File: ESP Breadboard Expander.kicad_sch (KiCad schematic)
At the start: 18 parts, among them J1 Conn_02x04_Odd_Even, J10 PJ-063BH, J2 Conn_01x08_Socket, J3 Conn_01x08_Socket, J4 Conn_01x19_Socket, J5 Conn_01x19_Socket, J6 Conn_01x14_Pin, J7 Conn_01x14_Pin, J8 Conn_01x02_Socket, J9 Conn_01x02_Socket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

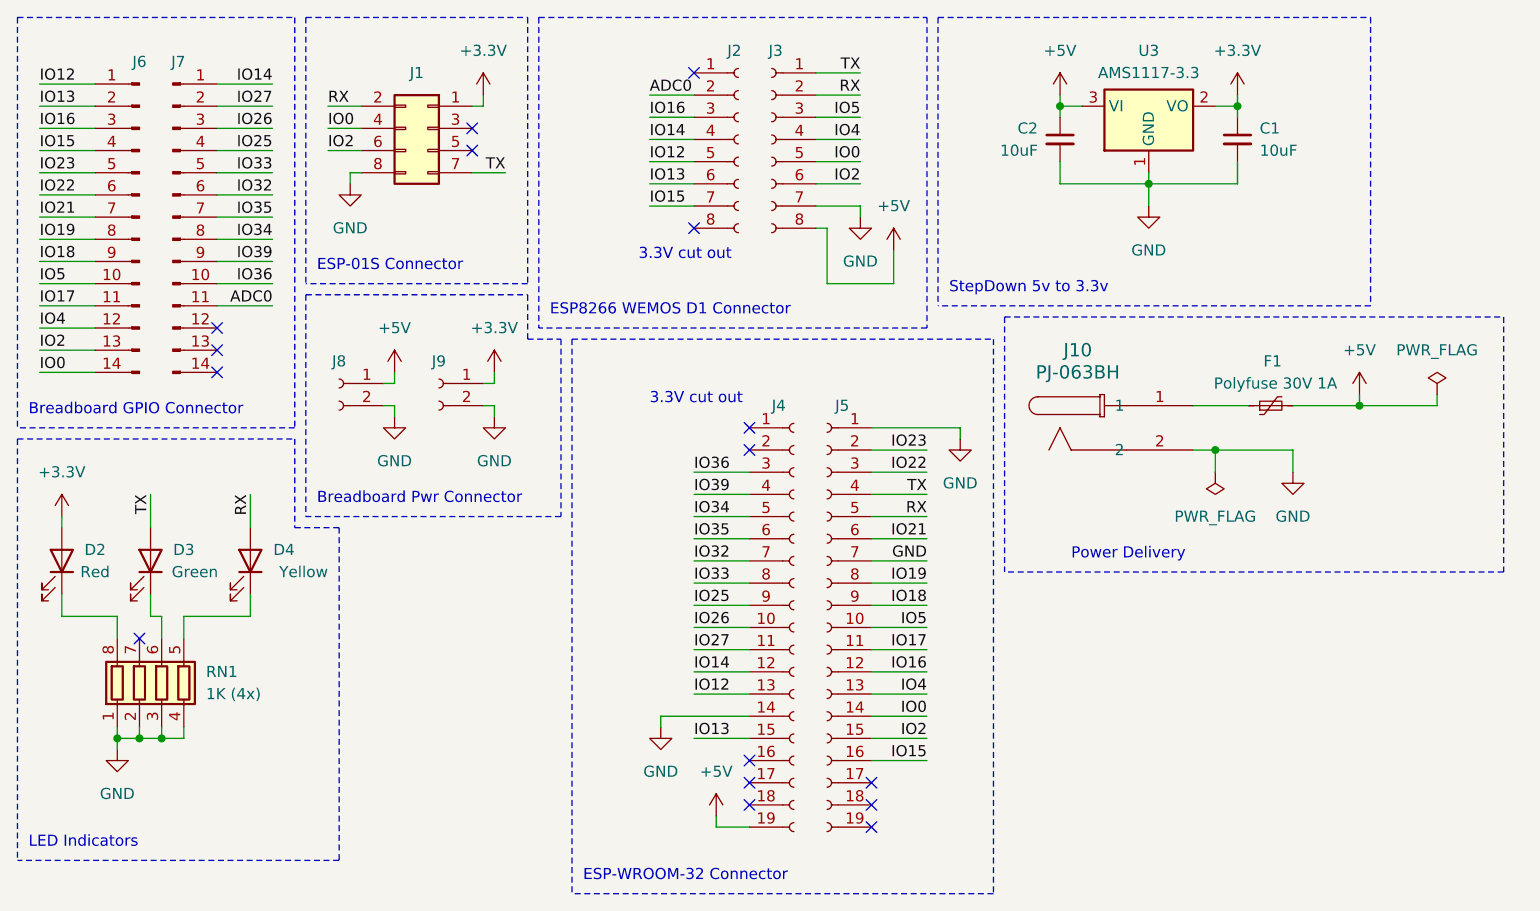
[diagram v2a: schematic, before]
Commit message: Fixed LED circuit & position of them
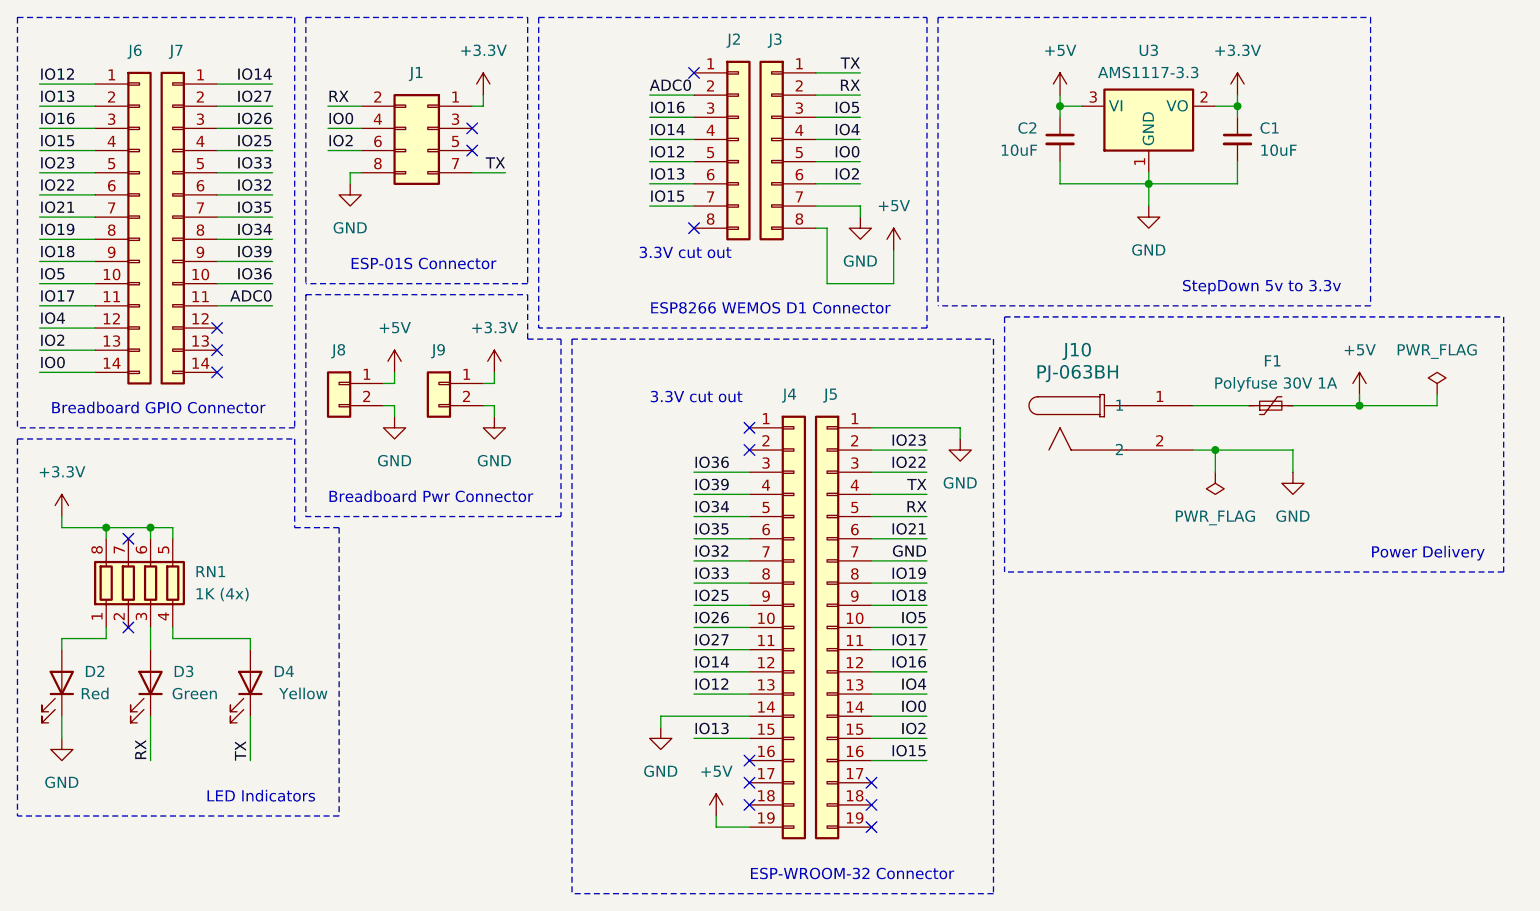
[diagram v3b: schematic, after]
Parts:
- removed J2, J3: Conn_01x08_Socket, Connector_PinSocket_2.54mm:PinSocket_1x08_P2.54mm_Vertical, symbol Connector:Conn_01x08_Socket
- removed J4, J5: Conn_01x19_Socket, Connector_PinSocket_2.54mm:PinSocket_1x19_P2.54mm_Vertical, symbol Connector:Conn_01x19_Socket
- removed J6, J7: Conn_01x14_Pin, Adam_Custom_Footprints:PinHeader_1x14_P2.54mm_Vertical_UpSideDown, symbol Connector:Conn_01x14_Pin
- removed J8, J9: Conn_01x02_Socket, Connector_PinSocket_2.54mm:PinSocket_1x02_P2.54mm_Vertical, symbol Connector:Conn_01x02_Socket
- added J2, J3: Conn_01x08_Socket, Connector_PinSocket_2.54mm:PinSocket_1x08_P2.54mm_Vertical, symbol Connector_Generic:Conn_01x08
- added J4, J5: Conn_01x19_Socket, Connector_PinSocket_2.54mm:PinSocket_1x19_P2.54mm_Vertical, symbol Connector_Generic:Conn_01x19
- added J6, J7: Conn_01x14_Pin, Adam_Custom_Footprints:PinHeader_1x14_P2.54mm_Vertical_UpSideDown, symbol Connector_Generic:Conn_01x14
- added J8, J9: Conn_01x02_Socket, Connector_PinSocket_2.54mm:PinSocket_1x02_P2.54mm_Vertical, symbol Connector_Generic:Conn_01x02
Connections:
- net +3.3V: now also RN1.5 (R4.2), RN1.6 (R3.2), RN1.8 (R1.2), J9.1 (Pin_1); no longer D2.2 (A)
- net +5V: now also J3.8 (Pin_8), J4.19 (Pin_19), J8.1 (Pin_1)
- net ADC0: now also J2.2 (Pin_2), J7.11 (Pin_11)
- net GND: now also D2.1 (K), J3.7 (Pin_7), J4.14 (Pin_14), J5.1 (Pin_1), J5.7 (Pin_7), J8.2 (Pin_2), J9.2 (Pin_2); no longer RN1.1 (R1.1), RN1.2 (R2.1), RN1.3 (R3.1), RN1.4 (R4.1)
- net IO0: now also J3.5 (Pin_5), J5.14 (Pin_14), J6.14 (Pin_14)
- net IO12: now also J2.5 (Pin_5), J4.13 (Pin_13), J6.1 (Pin_1)
- net IO13: now also J2.6 (Pin_6), J4.15 (Pin_15), J6.2 (Pin_2)
- net IO14: now also J2.4 (Pin_4), J4.12 (Pin_12), J7.1 (Pin_1)
- net IO15: now also J2.7 (Pin_7), J5.16 (Pin_16), J6.4 (Pin_4)
- net IO16: now also J2.3 (Pin_3), J5.12 (Pin_12), J6.3 (Pin_3)
- net IO17: now also J5.11 (Pin_11), J6.11 (Pin_11)
- net IO18: now also J5.9 (Pin_9), J6.9 (Pin_9)
- net IO19: now also J5.8 (Pin_8), J6.8 (Pin_8)
- net IO2: now also J3.6 (Pin_6), J5.15 (Pin_15), J6.13 (Pin_13)
- net IO21: now also J5.6 (Pin_6), J6.7 (Pin_7)
- net IO22: now also J5.3 (Pin_3), J6.6 (Pin_6)
- net IO23: now also J5.2 (Pin_2), J6.5 (Pin_5)
- net IO25: now also J4.9 (Pin_9), J7.4 (Pin_4)
- net IO26: now also J4.10 (Pin_10), J7.3 (Pin_3)
- net IO27: now also J4.11 (Pin_11), J7.2 (Pin_2)
- net IO32: now also J4.7 (Pin_7), J7.6 (Pin_6)
- net IO33: now also J4.8 (Pin_8), J7.5 (Pin_5)
- net IO34: now also J4.5 (Pin_5), J7.8 (Pin_8)
- net IO35: now also J4.6 (Pin_6), J7.7 (Pin_7)
- net IO36: now also J4.3 (Pin_3), J7.10 (Pin_10)
- net IO39: now also J4.4 (Pin_4), J7.9 (Pin_9)
- net IO4: now also J3.4 (Pin_4), J5.13 (Pin_13), J6.12 (Pin_12)
- net IO5: now also J3.3 (Pin_3), J5.10 (Pin_10), J6.10 (Pin_10)
- net RX: now also D3.1 (K), J3.2 (Pin_2), J5.5 (Pin_5); no longer D4.2 (A)
- net TX: now also D4.1 (K), J3.1 (Pin_1), J5.4 (Pin_4); no longer D3.2 (A)
- new net: D2.2 (A), RN1.1 (R1.1)
- new net: D3.2 (A), RN1.3 (R3.1)
- new net: D4.2 (A), RN1.4 (R4.1)
- no-connect marks 16 -> 17
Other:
- company: BroTech Industries, LLC -> (none)
- moved on the sheet: D2, D3, D4, RN1
